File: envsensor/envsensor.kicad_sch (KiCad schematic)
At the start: 1 part

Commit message: cleanup
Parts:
- removed U1: (no value), Library:esp32-s3-wroom-1-devkit, symbol New_Library:esp32-wroom-1-devkit
- added U1: (no value), ld2450:ld2450, symbol ld2450:ld2450
- added U2: (no value), Library:esp32-s3-wroom-1-devkit, symbol New_Library:esp32-wroom-1-devkit
- added U3: SCD30, kicad-libraries:SCD30, symbol tinkerforge:SCD30
- added U4: MS5611-01BA, Library:MS5611, symbol Sensor_Pressure:MS5611-01BA
- added U5: BH1750, Library:Untitled_1, symbol bh1750:_1
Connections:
- new net: U1.3 (TX), U2. (14)
- new net: U1.4 (RX), U2. (14)
- new net: U4.4 (CSB), U4.5 (CSB)
- new net 3V3: U1.6 (3V3), U2. (14), U3.1 (VDD)
- new net GND: U1.8 (GND), U2. (14), U3.2 (GND)

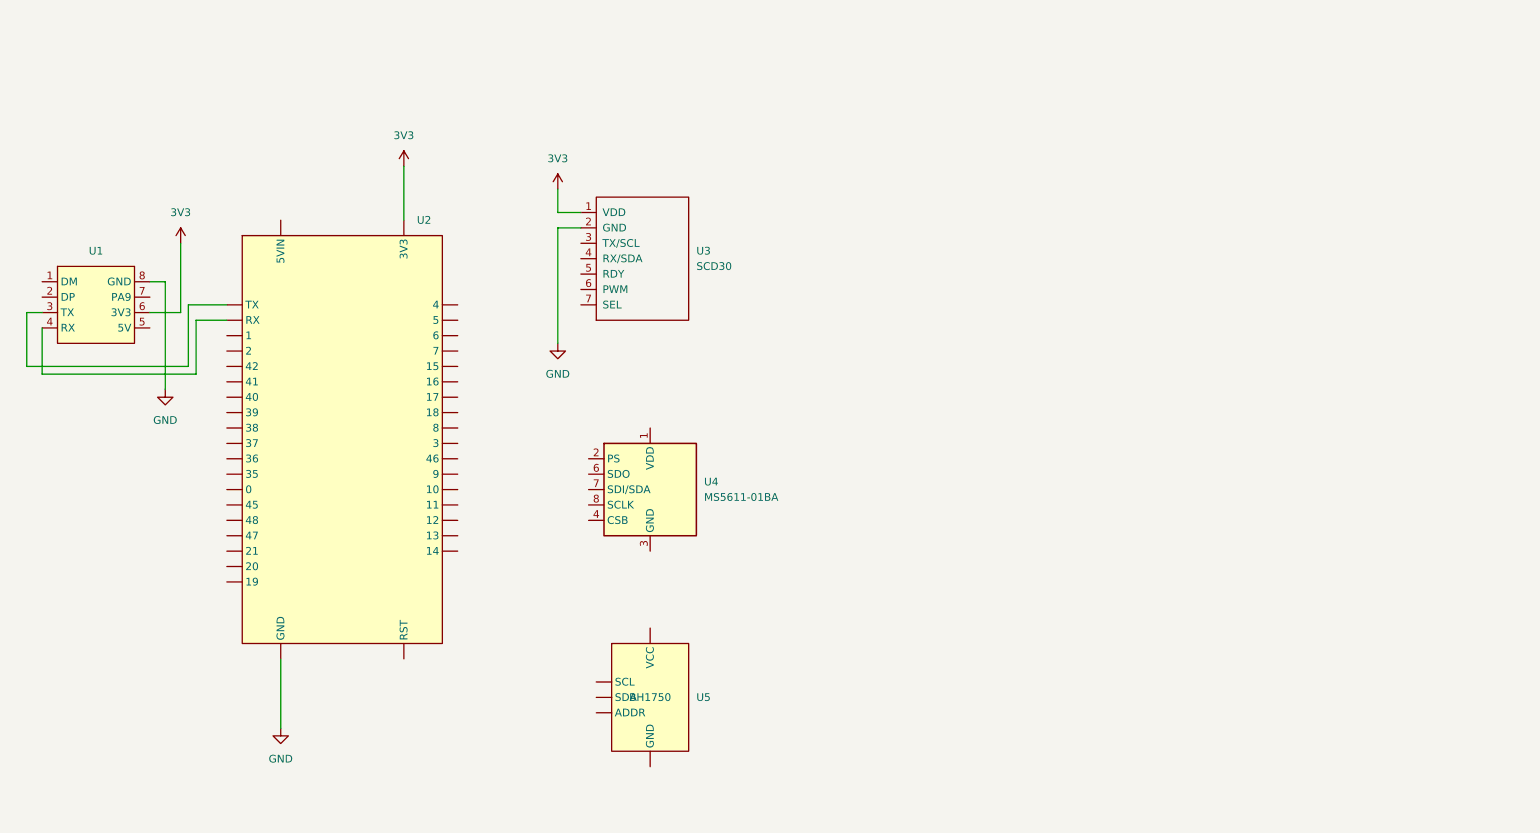
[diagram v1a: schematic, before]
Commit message: added led screen
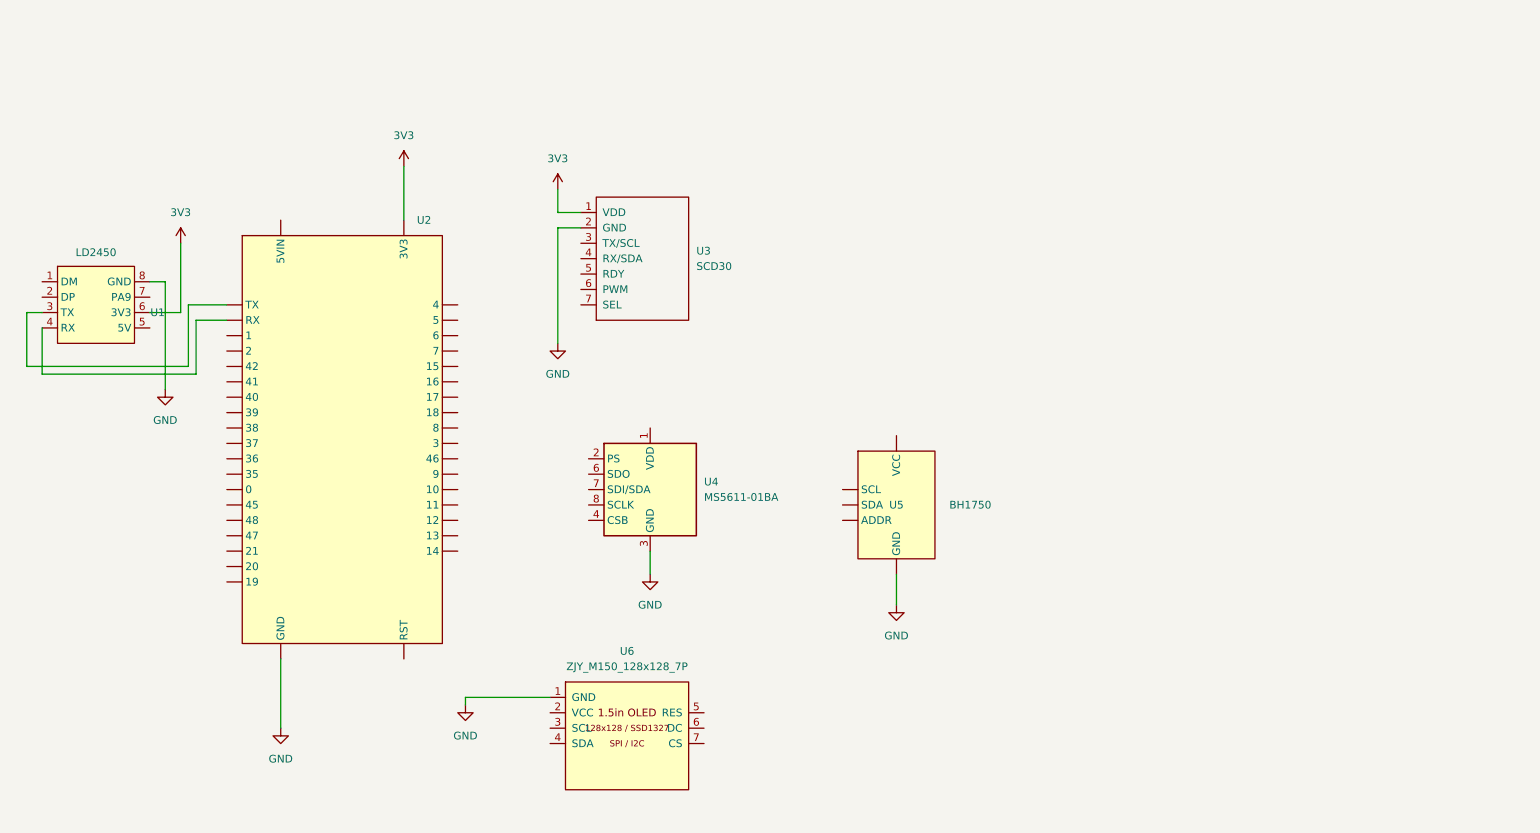
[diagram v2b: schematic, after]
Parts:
- added U6: ZJY_M150_128x128_7P, ZJY_M150_128x128_7P:ZJY_M150_128x128_7P, symbol SSD1327_ZJY_M150:ZJY_M150_128x128_7P
- U1: value (none) -> LD2450
- U3: footprint kicad-libraries:SCD30 -> (none)
- U4: footprint Library:MS5611 -> Package_LGA:LGA-8_3x5mm_P1.25mm
- U5: footprint Library:Untitled_1 -> Library:BH1750
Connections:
- net GND: now also U4.3 (GND), U5. (GND), U6.1 (GND)
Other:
- moved on the sheet: U5

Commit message: final version
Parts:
- removed U6: ZJY_M150_128x128_7P, ZJY_M150_128x128_7P:ZJY_M150_128x128_7P, symbol SSD1327_ZJY_M150:ZJY_M150_128x128_7P
- added J1: Conn_01x05, Connector_PinHeader_2.54mm:PinHeader_1x05_P2.54mm_Vertical, symbol Connector_Generic:Conn_01x05
- added R1, R2: 4K7, Resistor_SMD:R_0603_1608Metric, symbol Device:R_Small
- added U6: ZJY_M150_128x128_7P, Library:ZJY_M150_128x128_7P, symbol New_Library:ZJY_M150_128x128_7P
- U1: value LD2450 -> (none)
- U4: value MS5611-01BA -> MS5611; footprint Package_LGA:LGA-8_3x5mm_P1.25mm -> (none); symbol Sensor_Pressure:MS5611-01BA -> New_Library:MS5611
- U5: symbol bh1750:_1 -> New_Library:BH1750
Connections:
- net 3V3: now also U2.1 (3V3), U2.2 (3V3), U4.1 (VCC), U4.5 (CSB), U4.7 (PS), U5.5 (VCC), R1.2, R2.2, U6.2 (VCC); no longer U1.6 (3V3), U2. (14), U3.1 (VDD)
- net GND: now also U2.22 (GND), U2.23 (GND), U2.43 (GND), U2.44 (GND), U3.7 (SEL), U4.2 (GND), U5.1 (ADDR), U5.4 (GND), J1.2 (Pin_2), J1.5 (Pin_5), U6.1 (GND); no longer U2. (14), U4.3 (GND), U5. (GND)
- net ESP32RX: now reaches U1.3 (TX)
- net ESP32RX: now also U2.11 (18); no longer U2. (14)
- net ESP32TX: now reaches U1.4 (RX)
- net ESP32TX: now also U2.10 (17); no longer U2. (14)
- net SDA: now reaches U4.4 (SDA)
- net SDA: now also U2.12 (8), U3.4 (RX/SDA), U5.2 (SDA), J1.3 (Pin_3), R1.1; no longer U4.5 (CSB)
- net SCL: now reaches U3.3 (TX/SCL)
- net SCL: now also U2.15 (9), U4.3 (SCL), U5.3 (SCL), J1.4 (Pin_4), R2.1
- new net +5V: J1.1 (Pin_1), U1.6 (3V3), U2.21 (5VIN), U3.1 (VDD)
- new net ESP10: U2.16 (10), U6.7 (CS)
- new net ESP11: U2.17 (11), U6.4 (SDA)
- new net ESP12: U2.18 (12), U6.3 (SCL)
- new net ESP13: U2.19 (13), U6.6 (DC)
- new net ESP14: U2.20 (14), U6.5 (RES)
- no-connect marks 0 -> 35
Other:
- moved on the sheet: U1, U4
